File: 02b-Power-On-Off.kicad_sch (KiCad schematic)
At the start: 13 parts, among them Q2 BSS138, Q3 DMG2305UX-7, Q4 DMG2305UX-7, SW5 SW_Push

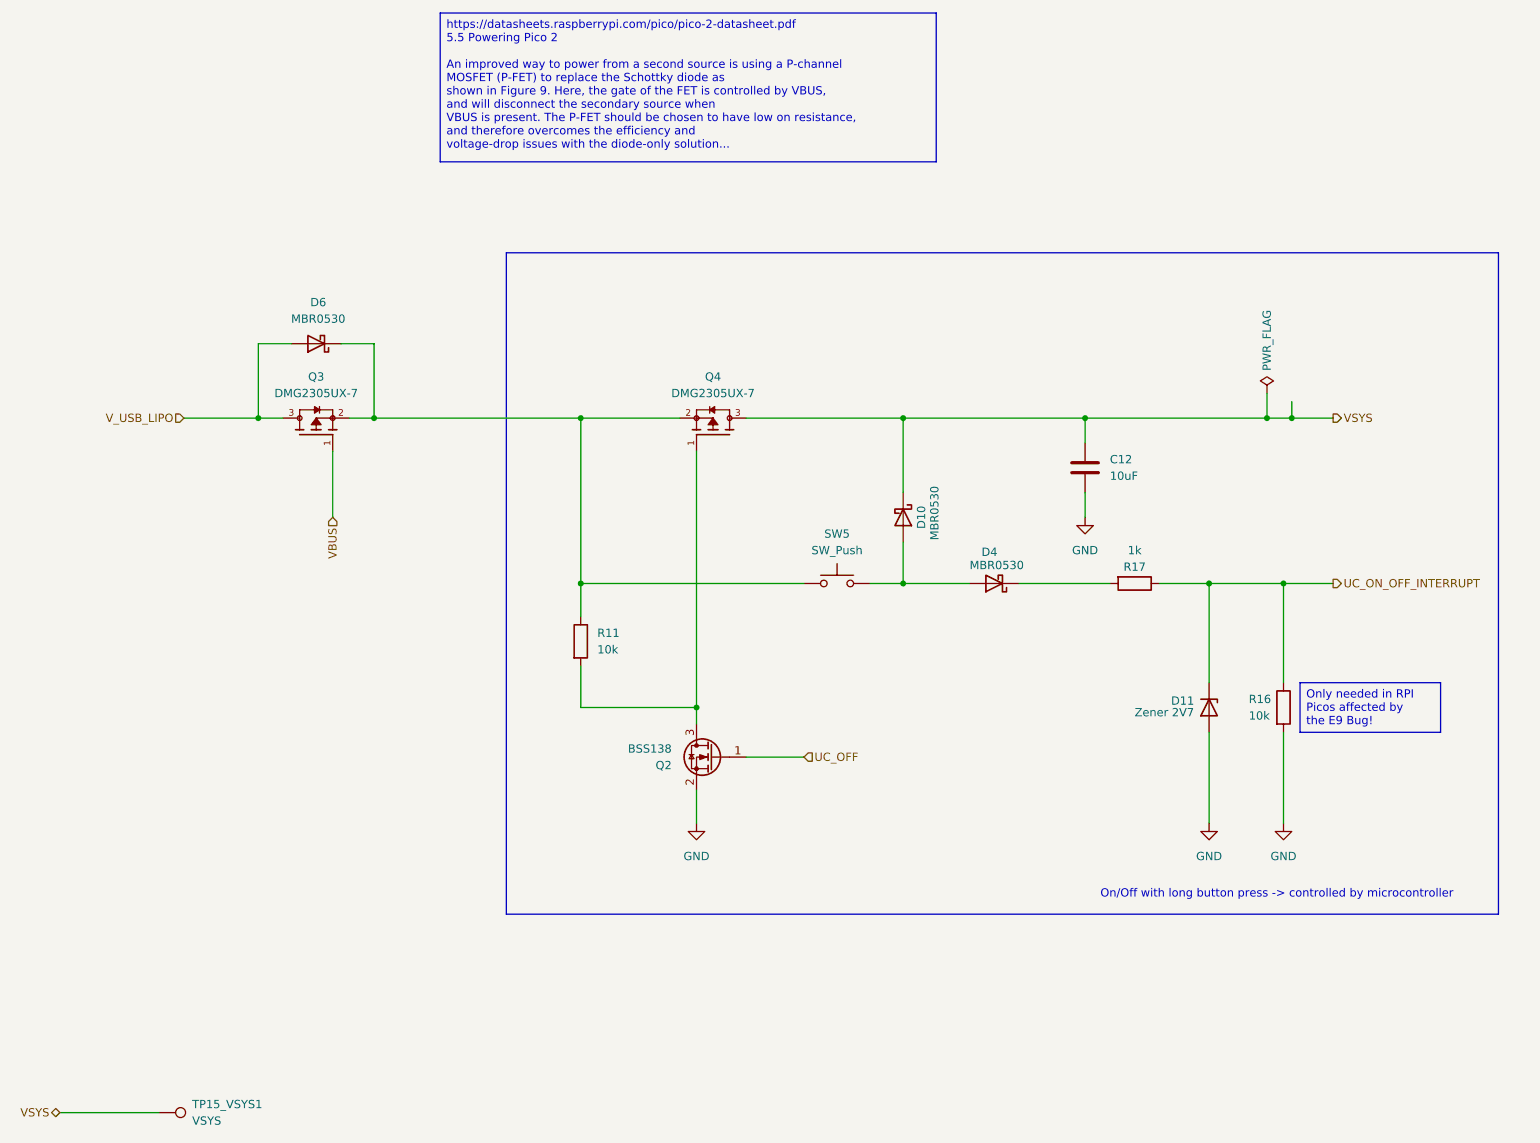
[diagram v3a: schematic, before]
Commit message: Reworked v2 routing
- some general improvements
- reworked component numbering
- routed and tuned differential pair (USB)
- added stiching vias and improved ground fills
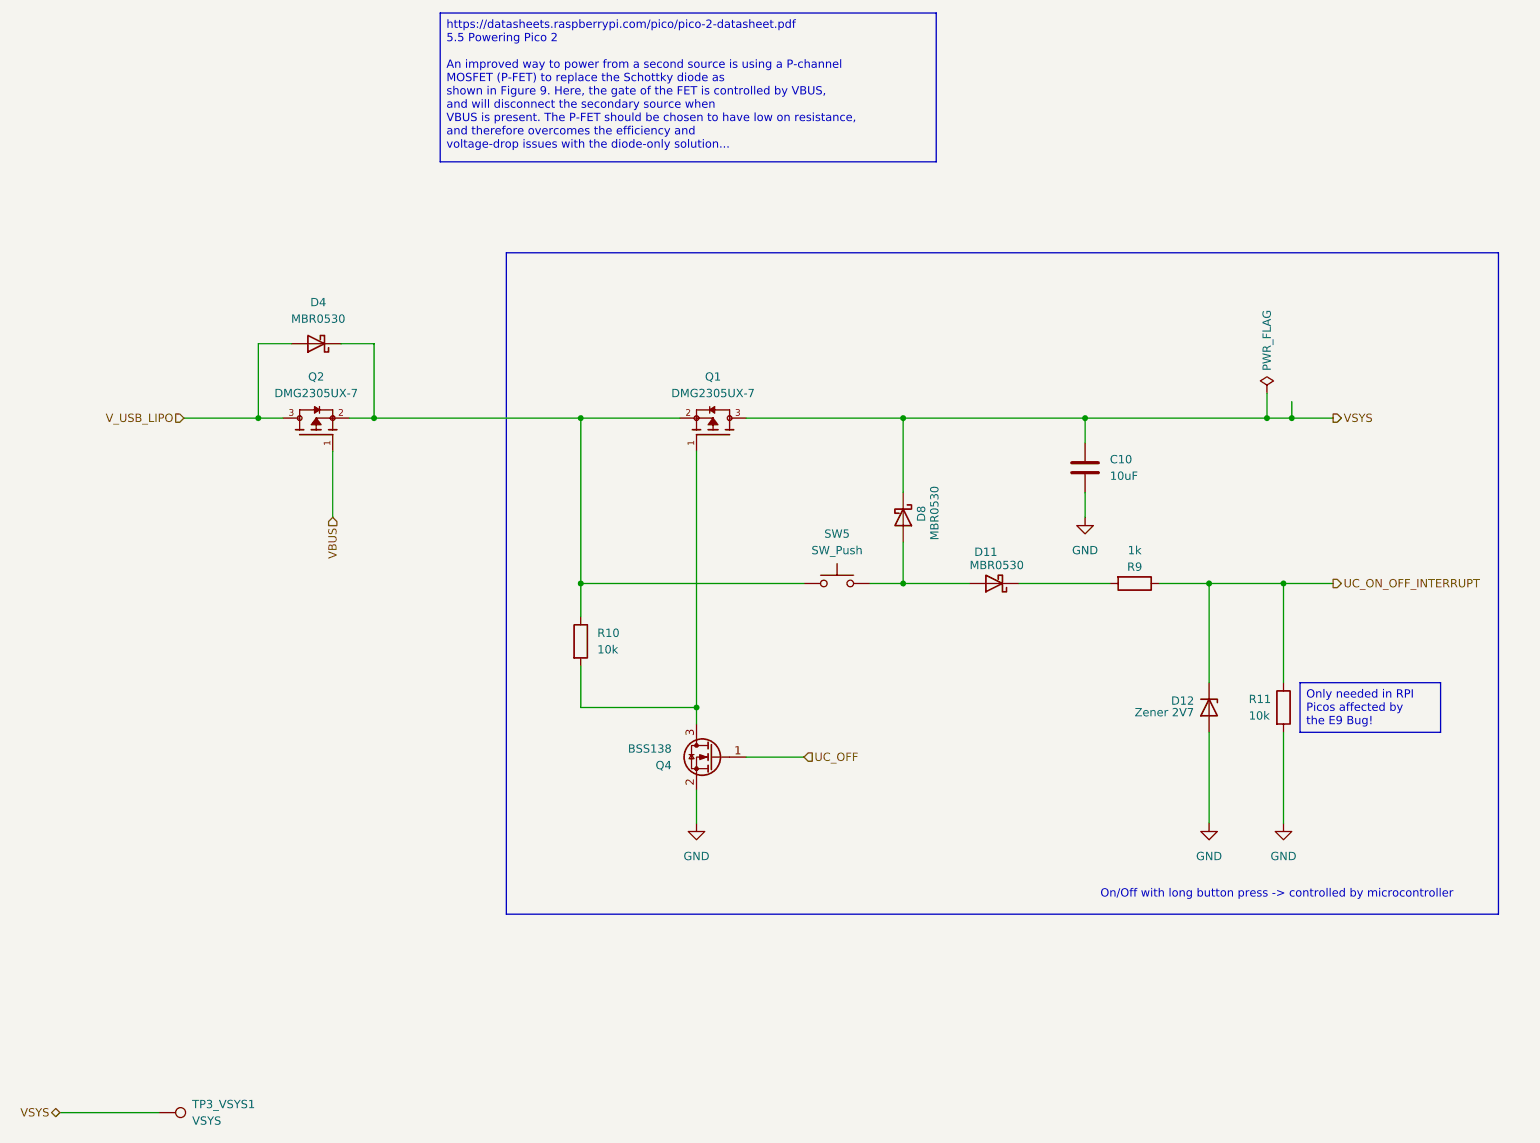
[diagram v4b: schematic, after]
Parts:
- renumbered C12 to C10, D4 to D11, D11 to D12, D6 to D4, D10 to D8, Q4 to Q1, Q3 to Q2, Q2 to Q4, R11 to R10, R16 to R11, R17 to R9, TP15_VSYS1 to TP3_VSYS1
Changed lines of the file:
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@@
 		(on_board yes)
 		(dnp no)
-		(property "Reference" "R16"
+		(property "Reference" "R11"
 			(at 215.646 119.38 0)
 			(effects
@@
 			(project ""
 				(path "/ec954637-2a8b-4662-b4a1-f88107f11cb0/a3bedda0-cdd4-4cf1-8725-53db0608a498"
-					(reference "R16")
+					(reference "R11")
 					(unit 1)
 				)
@@
 		(on_board yes)
 		(dnp no)
-		(property "Reference" "D4"
+		(property "Reference" "D11"
 			(at 177.038 96.774 0)
 			(effects
@@
 			(project "ZEReader-Pico"
 				(path "/ec954637-2a8b-4662-b4a1-f88107f11cb0/a3bedda0-cdd4-4cf1-8725-53db0608a498"
-					(reference "D4")
+					(reference "D11")
 					(unit 1)
 				)
@@
 		(dnp no)
 		(fields_autoplaced yes)
-		(property "Reference" "R11"
+		(property "Reference" "R10"
 			(at 115.57 109.2199 0)
 			(effects
@@
 			(project ""
 				(path "/ec954637-2a8b-4662-b4a1-f88107f11cb0/a3bedda0-cdd4-4cf1-8725-53db0608a498"
-					(reference "R11")
+					(reference "R10")
 					(unit 1)
 				)
@@
 		(on_board yes)
 		(dnp no)
-		(property "Reference" "Q4"
+		(property "Reference" "Q1"
 			(at 133.35 69.85 90)
 			(effects
@@
 			(project ""
 				(path "/ec954637-2a8b-4662-b4a1-f88107f11cb0/a3bedda0-cdd4-4cf1-8725-53db0608a498"
-					(reference "Q4")
+					(reference "Q1")
 					(unit 1)
 				)
@@
 		(dnp no)
 		(fields_autoplaced yes)
-		(property "Reference" "Q3"
+		(property "Reference" "Q2"
 			(at 72.39 69.85 90)
 			(effects
@@
 			(project ""
 				(path "/ec954637-2a8b-4662-b4a1-f88107f11cb0/a3bedda0-cdd4-4cf1-8725-53db0608a498"
-					(reference "Q3")
+					(reference "Q2")
 					(unit 1)
 				)
@@
 		(on_board yes)
 		(dnp no)
-		(property "Reference" "D10"
+		(property "Reference" "D8"
 			(at 165.354 89.662 0)
 			(effects
@@
 			(project "ZEReader-Pico"
 				(path "/ec954637-2a8b-4662-b4a1-f88107f11cb0/a3bedda0-cdd4-4cf1-8725-53db0608a498"
-					(reference "D10")
+					(reference "D8")
 					(unit 1)
 				)
@@
 		(on_board yes)
 		(dnp no)
-		(property "Reference" "Q2"
+		(property "Reference" "Q4"
 			(at 127 129.5401 0)
 			(effects
@@
 			(project "ZEReader-Pico"
 				(path "/ec954637-2a8b-4662-b4a1-f88107f11cb0/a3bedda0-cdd4-4cf1-8725-53db0608a498"
-					(reference "Q2")
+					(reference "Q4")
 					(unit 1)
 				)
@@
 		(on_board yes)
 		(dnp no)
-		(property "Reference" "C12"
+		(property "Reference" "C10"
 			(at 194.31 82.5499 0)
 			(effects
@@
 			(project "ZEReader-Pico"
 				(path "/ec954637-2a8b-4662-b4a1-f88107f11cb0/a3bedda0-cdd4-4cf1-8725-53db0608a498"
-					(reference "C12")
+					(reference "C10")
 					(unit 1)
 				)
@@
 		(on_board yes)
 		(dnp no)
-		(property "Reference" "R17"
+		(property "Reference" "R9"
 			(at 198.12 99.06 90)
 			(effects
@@
 			(project ""
 				(path "/ec954637-2a8b-4662-b4a1-f88107f11cb0/a3bedda0-cdd4-4cf1-8725-53db0608a498"
-					(reference "R17")
+					(reference "R9")
 					(unit 1)
 				)
@@
 		(dnp no)
 		(fields_autoplaced yes)
-		(property "Reference" "D6"
+		(property "Reference" "D4"
 			(at 72.7075 58.42 0)
 			(effects
@@
 			(project "ZEReader-Pico"
 				(path "/ec954637-2a8b-4662-b4a1-f88107f11cb0/a3bedda0-cdd4-4cf1-8725-53db0608a498"
-					(reference "D6")
+					(reference "D4")
 					(unit 1)
 				)
@@
 		(on_board yes)
 		(dnp no)
-		(property "Reference" "D11"
+		(property "Reference" "D12"
 			(at 203.708 119.634 90)
 			(effects
@@
 			(project ""
 				(path "/ec954637-2a8b-4662-b4a1-f88107f11cb0/a3bedda0-cdd4-4cf1-8725-53db0608a498"
-					(reference "D11")
+					(reference "D12")
 					(unit 1)
 				)
@@
 		(dnp no)
 		(fields_autoplaced yes)
-		(property "Reference" "TP15_VSYS1"
+		(property "Reference" "TP3_VSYS1"
 			(at 53.34 181.6099 90)
 			(effects
@@
 			(project "ZEReader-Pico"
 				(path "/ec954637-2a8b-4662-b4a1-f88107f11cb0/a3bedda0-cdd4-4cf1-8725-53db0608a498"
-					(reference "TP15_VSYS1")
-					(unit 1)
-				)
+					(reference "TP3_VSYS1")
+					(unit 1)
+				)

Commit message: some minor improvements after evaluating the CI run
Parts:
- Q1, Q2: footprint Package_TO_SOT_SMD:SOT-23-3 -> DMG2305UX-7:SOT91P240X110-3N_DMG2305UX-7
- TP3_VSYS1: now left out of the parts list
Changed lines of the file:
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@@
 	(generator_version "9.0")
 	(paper "A4")
+	(title_block
+		(rev "v2")
+	)
 	(rectangle
 		(start 101.6 50.8)
@@
 			)
 		)
-		(property "Footprint" "Package_TO_SOT_SMD:SOT-23-3"
+		(property "Footprint" "DMG2305UX-7:SOT91P240X110-3N_DMG2305UX-7"
 			(at 133.35 78.74 0)
 			(effects
@@
 			)
 		)
-		(property "Footprint" "Package_TO_SOT_SMD:SOT-23-3"
+		(property "Footprint" "DMG2305UX-7:SOT91P240X110-3N_DMG2305UX-7"
 			(at 72.39 78.74 0)
 			(effects
@@
 		(unit 1)
 		(exclude_from_sim no)
-		(in_bom yes)
+		(in_bom no)
 		(on_board yes)
 		(dnp no)

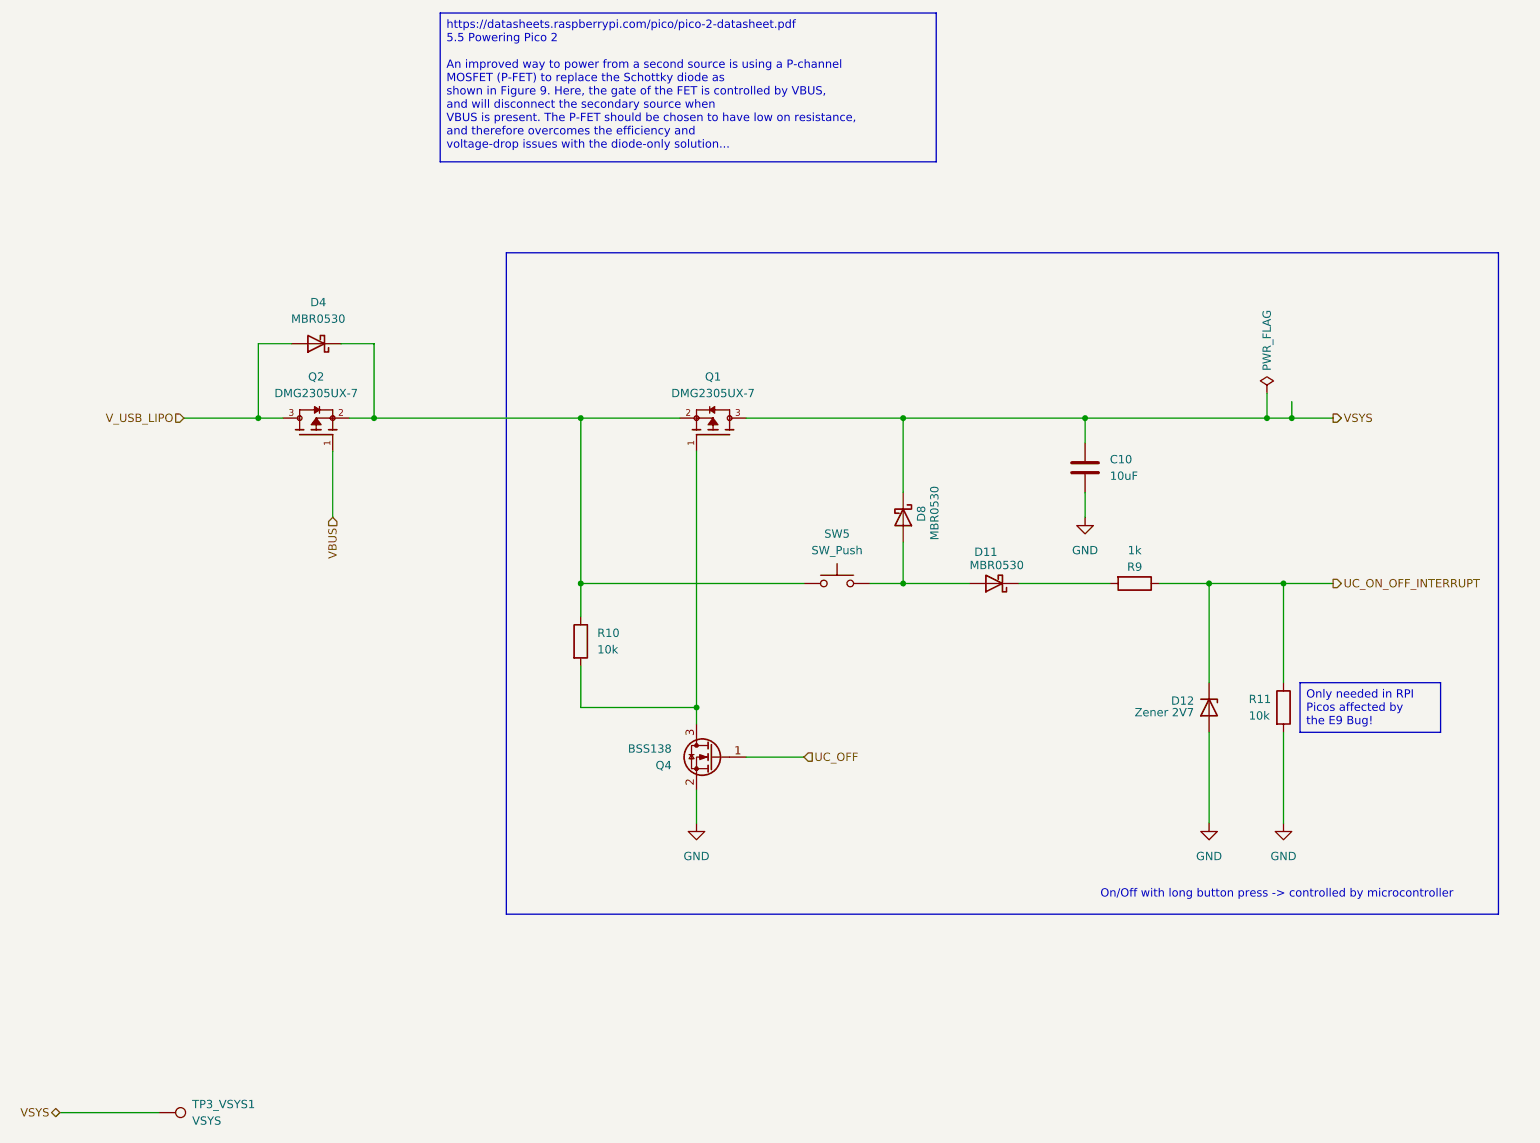
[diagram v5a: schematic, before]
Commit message: v2: final touch
- add proper ESD diodes for USB
- move the USB fuse right after the connector
- pretty labels for test points
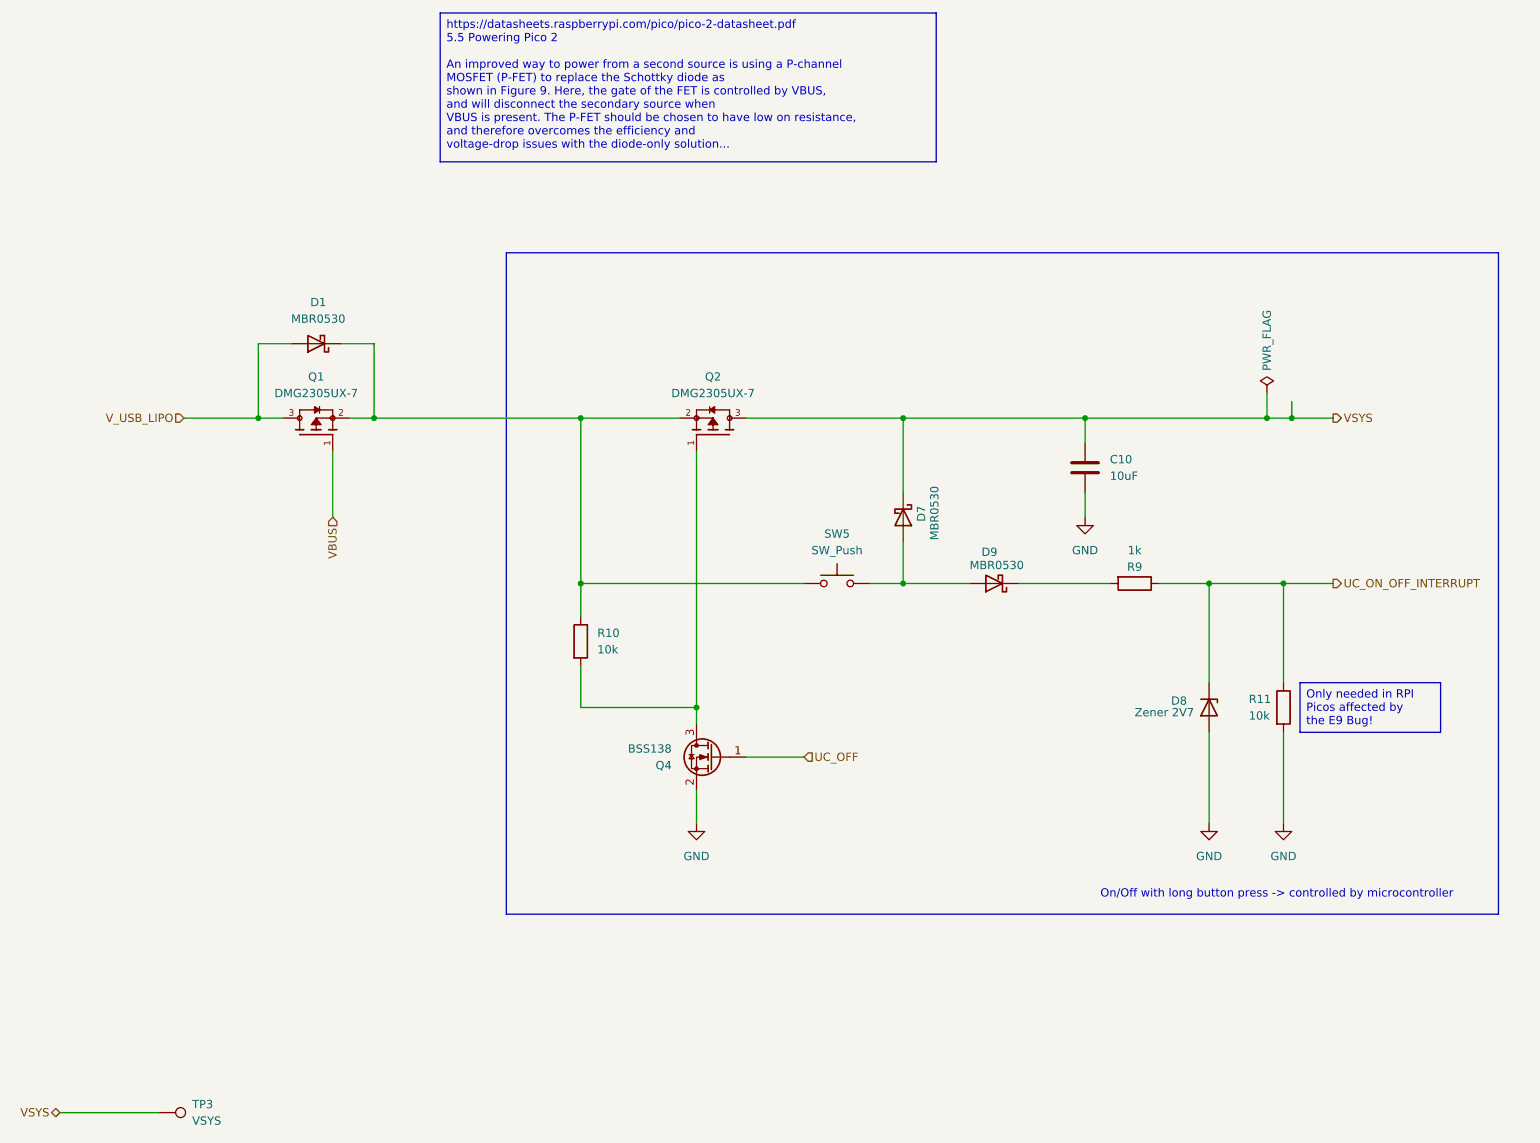
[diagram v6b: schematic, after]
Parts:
- Q1: renamed from Q2; footprint DMG2305UX-7:SOT91P240X110-3N_DMG2305UX-7 -> Package_TO_SOT_SMD:SOT-23-3
- Q2: renamed from Q1; footprint DMG2305UX-7:SOT91P240X110-3N_DMG2305UX-7 -> Package_TO_SOT_SMD:SOT-23-3
- renumbered D4 to D1, D8 to D7, D12 to D8, D11 to D9, TP3_VSYS1 to TP3
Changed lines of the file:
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@@
 		(on_board yes)
 		(dnp no)
-		(property "Reference" "D11"
+		(property "Reference" "D9"
 			(at 177.038 96.774 0)
 			(effects
@@
 			(project "ZEReader-Pico"
 				(path "/ec954637-2a8b-4662-b4a1-f88107f11cb0/a3bedda0-cdd4-4cf1-8725-53db0608a498"
-					(reference "D11")
+					(reference "D9")
 					(unit 1)
 				)
@@
 		(on_board yes)
 		(dnp no)
-		(property "Reference" "Q1"
+		(property "Reference" "Q2"
 			(at 133.35 69.85 90)
 			(effects
@@
 			)
 		)
-		(property "Footprint" "DMG2305UX-7:SOT91P240X110-3N_DMG2305UX-7"
+		(property "Footprint" "Package_TO_SOT_SMD:SOT-23-3"
 			(at 133.35 78.74 0)
 			(effects
@@
 			(project ""
 				(path "/ec954637-2a8b-4662-b4a1-f88107f11cb0/a3bedda0-cdd4-4cf1-8725-53db0608a498"
-					(reference "Q1")
+					(reference "Q2")
 					(unit 1)
 				)
@@
 		(dnp no)
 		(fields_autoplaced yes)
-		(property "Reference" "Q2"
+		(property "Reference" "Q1"
 			(at 72.39 69.85 90)
 			(effects
@@
 			)
 		)
-		(property "Footprint" "DMG2305UX-7:SOT91P240X110-3N_DMG2305UX-7"
+		(property "Footprint" "Package_TO_SOT_SMD:SOT-23-3"
 			(at 72.39 78.74 0)
 			(effects
@@
 			(project ""
 				(path "/ec954637-2a8b-4662-b4a1-f88107f11cb0/a3bedda0-cdd4-4cf1-8725-53db0608a498"
-					(reference "Q2")
+					(reference "Q1")
 					(unit 1)
 				)
@@
 		(on_board yes)
 		(dnp no)
-		(property "Reference" "D8"
+		(property "Reference" "D7"
 			(at 165.354 89.662 0)
 			(effects
@@
 			(project "ZEReader-Pico"
 				(path "/ec954637-2a8b-4662-b4a1-f88107f11cb0/a3bedda0-cdd4-4cf1-8725-53db0608a498"
-					(reference "D8")
+					(reference "D7")
 					(unit 1)
 				)
@@
 		(dnp no)
 		(fields_autoplaced yes)
-		(property "Reference" "D4"
+		(property "Reference" "D1"
 			(at 72.7075 58.42 0)
 			(effects
@@
 			(project "ZEReader-Pico"
 				(path "/ec954637-2a8b-4662-b4a1-f88107f11cb0/a3bedda0-cdd4-4cf1-8725-53db0608a498"
-					(reference "D4")
+					(reference "D1")
 					(unit 1)
 				)
@@
 		(on_board yes)
 		(dnp no)
-		(property "Reference" "D12"
+		(property "Reference" "D8"
 			(at 203.708 119.634 90)
 			(effects
@@
 			(project ""
 				(path "/ec954637-2a8b-4662-b4a1-f88107f11cb0/a3bedda0-cdd4-4cf1-8725-53db0608a498"
-					(reference "D12")
+					(reference "D8")
 					(unit 1)
 				)
@@
 		(dnp no)
 		(fields_autoplaced yes)
-		(property "Reference" "TP3_VSYS1"
+		(property "Reference" "TP3"
 			(at 53.34 181.6099 90)
 			(effects
@@
 			(project "ZEReader-Pico"
 				(path "/ec954637-2a8b-4662-b4a1-f88107f11cb0/a3bedda0-cdd4-4cf1-8725-53db0608a498"
-					(reference "TP3_VSYS1")
-					(unit 1)
-				)
+					(reference "TP3")
+					(unit 1)
+				)
